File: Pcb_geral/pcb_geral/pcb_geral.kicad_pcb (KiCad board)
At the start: 2 copper layers, 62.5 x 34.8 mm, 21 parts, among them U1 LM2594M-3.3, U2 LM2596S-5, U3 STM32F103C6Tx, U4 TJA1051T, Y2 8Mhz

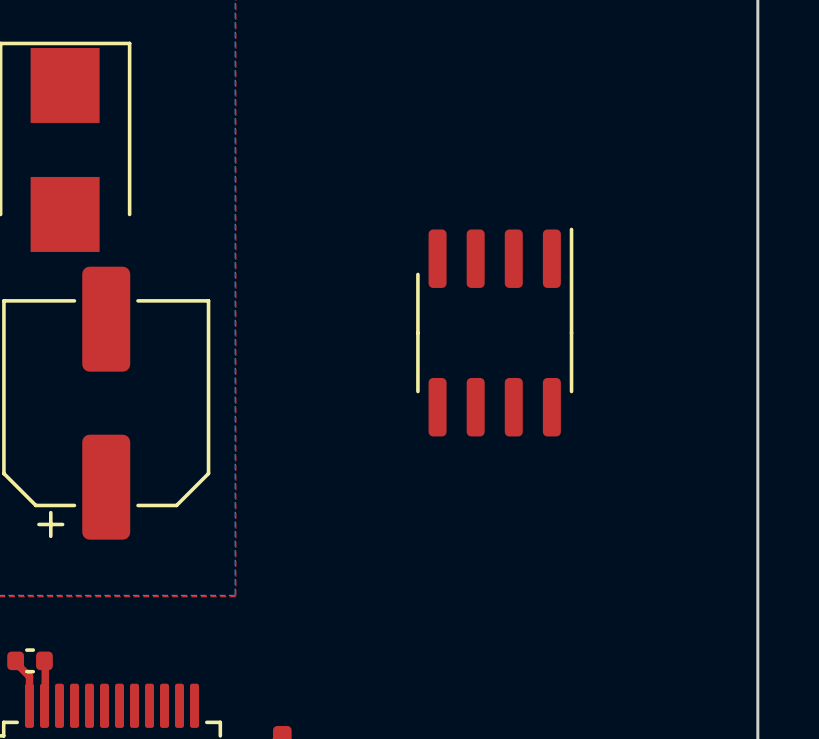
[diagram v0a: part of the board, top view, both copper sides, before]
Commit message: placa geral, add can e footprints
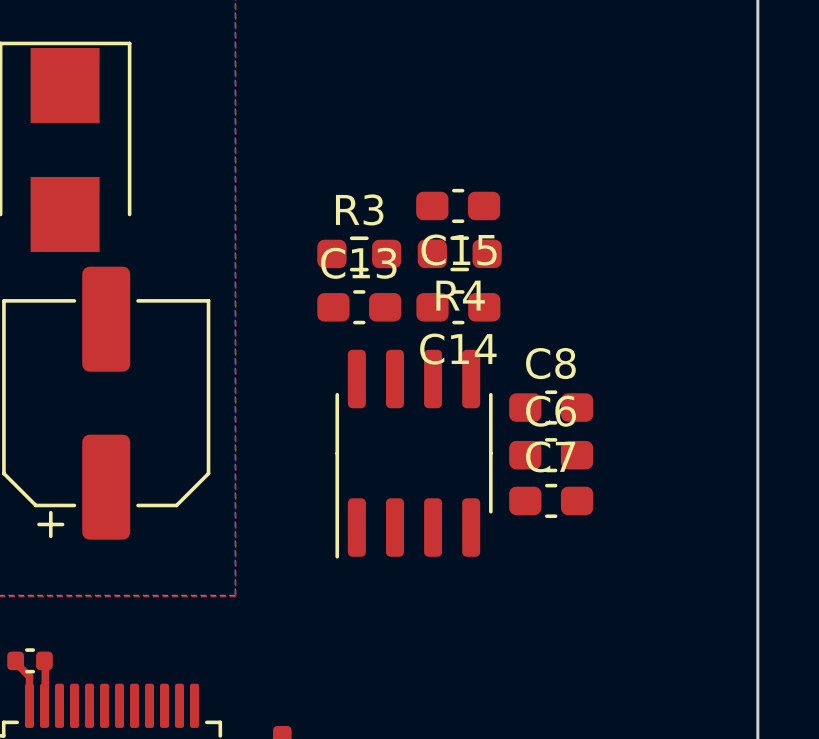
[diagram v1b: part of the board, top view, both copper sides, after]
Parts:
- added C13: 100pF, Capacitor_SMD:C_0603_1608Metric_Pad1.08x0.95mm_HandSolder, F.Cu at (119.8, 49.4)
- added C14: 100pF, Capacitor_SMD:C_0603_1608Metric_Pad1.08x0.95mm_HandSolder, F.Cu at (123.1, 49.4)
- added C15: 4,7uF, Capacitor_SMD:C_0603_1608Metric_Pad1.08x0.95mm_HandSolder, F.Cu at (123.1, 46.1)
- added C6: 100nF, Capacitor_SMD:C_0603_1608Metric_Pad1.08x0.95mm_HandSolder, F.Cu at (126.2, 54.4)
- added C7: 47nF, Capacitor_SMD:C_0603_1608Metric_Pad1.08x0.95mm_HandSolder, F.Cu at (126.2, 55.9)
- added C8: 100µF, Capacitor_SMD:C_0603_1608Metric_Pad1.08x0.95mm_HandSolder, F.Cu at (126.2, 52.8)
- added R3: 60, Resistor_SMD:R_0603_1608Metric_Pad0.98x0.95mm_HandSolder, F.Cu at (119.8, 47.7)
- added R4: 60, Resistor_SMD:R_0603_1608Metric_Pad0.98x0.95mm_HandSolder, F.Cu at (123.1, 47.7)
- U4: value TJA1051T -> TJA1051T-3
- moved U4 4.83 mm to (121.6, 54.3), turned to 90 degrees
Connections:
- U3 pad 45: CANRX -> /Can+
- U3 pad 46: CANTX -> /Can-
- U4 pad 1: CANTX -> TxD
- U4 pad 4: CANRX -> RxD
- U4 pad 5: unconnected-(U4-Pad5) -> +3V3
- U4 pad 6: CAN- -> /Can-
- U4 pad 7: CAN+ -> /Can+
- U4 pad 8: unconnected-(U4-Pad8) -> EnableCan

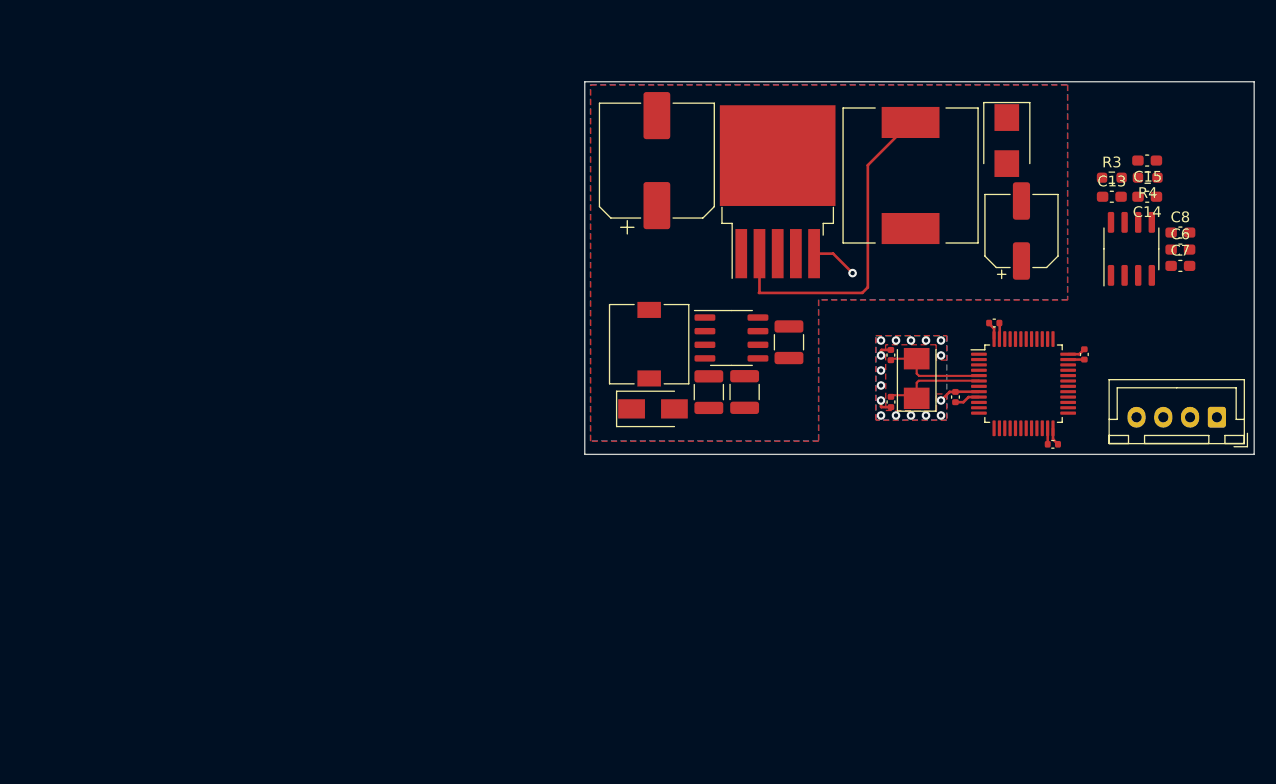
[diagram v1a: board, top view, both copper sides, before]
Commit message: atualizacoes na placa geral, posicionamento do can, adição dos pontos para conexão para sensores e dispositivos externos, sistemas de proteção contra corrente excessiva e reversão de tensão, silk mais detalhado entre outros
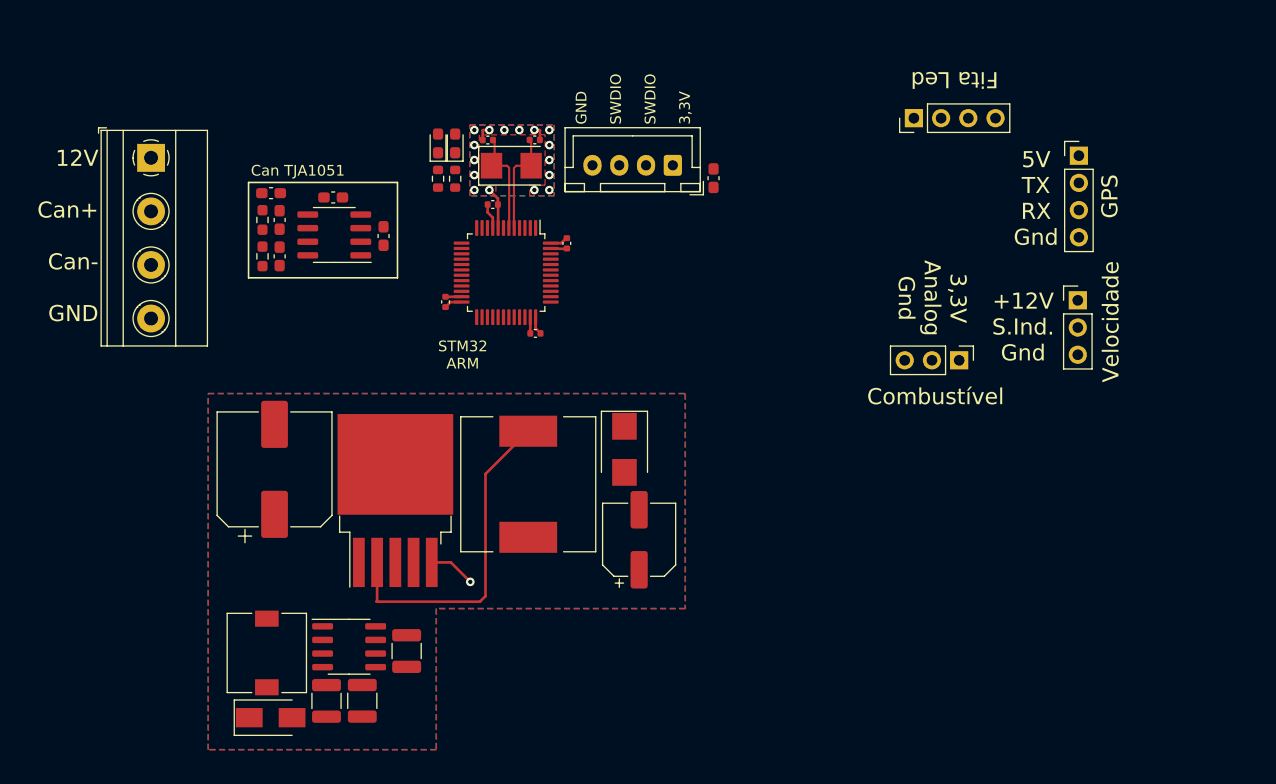
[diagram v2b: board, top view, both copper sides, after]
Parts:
- added D3: LED, LED_SMD:LED_0603_1608Metric_Pad1.05x0.95mm_HandSolder, F.Cu at (56.9, 44.5)
- added D4: LED, LED_SMD:LED_0603_1608Metric_Pad1.05x0.95mm_HandSolder, F.Cu at (58.5, 44.5)
- added J1: Conn_01x04_Female, TerminalBlock_Phoenix:TerminalBlock_Phoenix_MKDS-1,5-4_1x04_P5.00mm_Horizontal, F.Cu at (30.1, 45.8)
- added J2: Conn_01x03_Female, Connector_PinHeader_2.54mm:PinHeader_1x03_P2.54mm_Vertical, F.Cu at (116.6, 59.1)
- added J3: Conn_01x03_Female, Connector_PinHeader_2.54mm:PinHeader_1x03_P2.54mm_Vertical, F.Cu at (105.5, 64.7)
- added J5: Conn_01x04_Female, Connector_PinHeader_2.54mm:PinHeader_1x04_P2.54mm_Vertical, F.Cu at (116.7, 45.6)
- added J6: Conn_01x04_Female, Connector_PinHeader_2.54mm:PinHeader_1x04_P2.54mm_Vertical, F.Cu at (101.3, 42.1)
- added R1: 510, Resistor_SMD:R_0603_1608Metric, F.Cu at (56.9, 47.8)
- added R2: 510, Resistor_SMD:R_0603_1608Metric, F.Cu at (58.5, 47.8)
- moved R4 82.7 mm to (40.5, 51.6), turned to 90 degrees
- moved C15 81.8 mm to (41.3, 49.1)
- moved C14 81.0 mm to (42.1, 51.6), turned to -90 degrees
- moved R3 79.6 mm to (40.5, 55.0), turned to -90 degrees
- moved C6 79.2 mm to (47.1, 49.5)
- moved C13 77.9 mm to (42.1, 55.0), turned to 90 degrees
- moved C7 74.4 mm to (51.8, 53.1), turned to -90 degrees
- moved U4 74.4 mm to (47.2, 53.0), turned to 180 degrees
- moved C9 58.2 mm to (57.6, 59.2), turned to 90 degrees
- moved Prog1 56.0 mm to (78.8, 46.5)
- moved C12 51.3 mm to (66.0, 62.2), turned to 180 degrees
- moved U3 49.4 mm to (63.2, 56.5), turned to -90 degrees
- moved C10 46.8 mm to (62.0, 50.2), turned to 0 degrees
- moved C3 45.9 mm to (49.8, 96.5)
- moved C8 45.9 mm to (75.7, 81.5)
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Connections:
- U3 pad 45: /Can+ -> unconnected-(U3-Pad45)
- U3 pad 46: /Can- -> unconnected-(U3-Pad46)
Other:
- board outline removed
- board text added: "+12V S.Ind. Gnd"
- board text added: "12V Can+ Can- GND"
- board text added: "3,3V Analog Gnd"
- board text added: "5V TX RX Gnd"
- board text added: "Can TJA1051"
- board text added: "Combustível"
- board text added: "Fita Led"
- board text added: "GND SWDIO SWDIO 3,3V"
- board text added: "GPS"
- board text added: "STM32 ARM"
- board text added: "Velocidade"

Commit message: add 3d
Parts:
- renumbered C7 to C2, C8 to C4, D1 to D2
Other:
- board outline added: 107.1 x 69 mm
